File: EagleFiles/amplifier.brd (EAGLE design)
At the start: 100 x 80 mm, 52 parts, among them X1 736880-49

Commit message: Fix Feedback
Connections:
- removed net N$5: C2.-, R6.2, R7.1
- new net N$35: C2.+, EF86.3, R6.1
- new net N$36: EF86.8
- net N$3: now also C2.-, R6.2, R7.1; no longer C2.+, EF86.3, EF86.8, R6.1
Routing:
- net N$3: track 82.9 -> 32.7 mm
- net N$35: track 0.00 -> 49.0 mm, vias 0 -> 1
- net N$5: track 17.6 -> 0.00 mm
- net N$12: track 20.2 -> 26.5 mm
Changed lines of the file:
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@@
 <layer number="17" name="Pads" color="2" fill="1" visible="yes" active="yes"/>
 <layer number="18" name="Vias" color="2" fill="1" visible="yes" active="yes"/>
-<layer number="19" name="Unrouted" color="6" fill="1" visible="no" active="yes"/>
+<layer number="19" name="Unrouted" color="6" fill="1" visible="yes" active="yes"/>
 <layer number="20" name="Dimension" color="24" fill="1" visible="yes" active="yes"/>
 <layer number="21" name="tPlace" color="7" fill="1" visible="no" active="yes"/>
@@
 <wire x1="23.622" y1="25.146" x2="23.368" y2="24.826" width="1.016" layer="1"/>
 </signal>
-<signal name="N$3">
-<contactref element="EF86" pad="3"/>
-<contactref element="EF86" pad="8"/>
-<contactref element="R6" pad="1"/>
-<contactref element="R8" pad="1"/>
-<contactref element="C7" pad="1"/>
-<contactref element="C2" pad="+"/>
-<wire x1="15.24" y1="36.576" x2="15.24" y2="47.244" width="1.016" layer="1"/>
-<wire x1="19.812" y1="32.004" x2="15.24" y2="36.576" width="1.016" layer="1"/>
-<wire x1="15.24" y1="47.244" x2="14.633" y2="47.882" width="1.016" layer="1"/>
-<wire x1="19.812" y1="32.004" x2="20.137" y2="31.751" width="1.016" layer="1"/>
-<wire x1="36.576" y1="18.288" x2="32.766" y2="18.288" width="1.016" layer="1"/>
-<wire x1="32.766" y1="18.288" x2="32.512" y2="17.714" width="1.016" layer="1"/>
-<wire x1="36.576" y1="18.288" x2="37.084" y2="17.714" width="1.016" layer="1"/>
-<wire x1="44.196" y1="13.716" x2="47.752" y2="13.716" width="1.016" layer="1"/>
-<wire x1="40.386" y1="17.526" x2="44.196" y2="13.716" width="1.016" layer="1"/>
-<wire x1="37.338" y1="17.526" x2="40.386" y2="17.526" width="1.016" layer="1"/>
-<wire x1="37.338" y1="17.526" x2="37.084" y2="17.714" width="1.016" layer="1"/>
-<wire x1="41.402" y1="20.066" x2="47.752" y2="13.716" width="1.016" layer="16"/>
-<wire x1="41.402" y1="20.066" x2="31.242" y2="20.066" width="1.016" layer="16"/>
-<wire x1="20.574" y1="30.734" x2="20.574" y2="31.242" width="1.016" layer="16"/>
-<wire x1="28.702" y1="10.668" x2="28.702" y2="21.1836" width="1.016" layer="16"/>
-<wire x1="20.574" y1="31.242" x2="20.137" y2="31.751" width="1.016" layer="16"/>
-<wire x1="29.464" y1="21.844" x2="20.574" y2="30.734" width="1.016" layer="16"/>
-<wire x1="28.702" y1="21.1836" x2="29.3624" y2="21.844" width="1.016" layer="16"/>
-<wire x1="31.242" y1="20.066" x2="29.464" y2="21.844" width="1.016" layer="16"/>
-<wire x1="29.464" y1="21.844" x2="29.3624" y2="21.844" width="1.016" layer="16"/>
-</signal>
 <signal name="N$4">
 <contactref element="EF86" pad="1"/>
@@
 <wire x1="24.384" y1="44.958" x2="24.384" y2="45.085" width="1.016" layer="16"/>
 <wire x1="10.668" y1="35.052" x2="10.502" y2="34.874" width="1.016" layer="16"/>
-</signal>
-<signal name="N$5">
-<contactref element="R6" pad="2"/>
-<contactref element="R7" pad="1"/>
-<contactref element="C2" pad="-"/>
-<wire x1="34.29" y1="15.24" x2="32.766" y2="15.24" width="1.016" layer="1"/>
-<wire x1="38.862" y1="10.668" x2="34.29" y2="15.24" width="1.016" layer="1"/>
-<wire x1="32.766" y1="15.24" x2="32.512" y2="15.814" width="1.016" layer="1"/>
-<wire x1="28.194" y1="19.05" x2="25.334" y2="19.05" width="1.016" layer="1"/>
-<wire x1="32.004" y1="15.24" x2="28.194" y2="19.05" width="1.016" layer="1"/>
-<wire x1="32.004" y1="15.24" x2="32.512" y2="15.814" width="1.016" layer="1"/>
 </signal>
 <signal name="N$6">
@@
 </signal>
 <signal name="N$12">
-<contactref element="R8" pad="2"/>
-<contactref element="C7" pad="2"/>
 <contactref element="FEEDBACK" pad="1"/>
-<wire x1="40.386" y1="15.24" x2="37.338" y2="15.24" width="1.016" layer="1"/>
-<wire x1="47.244" y1="8.382" x2="40.386" y2="15.24" width="1.016" layer="1"/>
-<wire x1="37.338" y1="15.24" x2="37.084" y2="15.814" width="1.016" layer="1"/>
-<wire x1="47.244" y1="8.382" x2="47.752" y2="8.636" width="1.016" layer="1"/>
 <wire x1="48.006" y1="8.382" x2="48.006" y2="3.048" width="1.016" layer="1"/>
 <wire x1="48.006" y1="3.048" x2="48.26" y2="2.54" width="1.016" layer="1"/>
-<wire x1="48.006" y1="8.382" x2="47.752" y2="8.636" width="1.016" layer="1"/>
+<contactref element="C7" pad="2"/>
+<contactref element="R8" pad="2"/>
+<wire x1="47.752" y1="8.636" x2="50.038" y2="10.922" width="0.762" layer="1"/>
+<wire x1="50.038" y1="14.986" x2="49.53" y2="15.494" width="0.762" layer="1"/>
+<wire x1="37.404" y1="15.494" x2="37.084" y2="15.814" width="0.762" layer="1"/>
+<wire x1="50.038" y1="10.922" x2="50.038" y2="14.986" width="0.762" layer="1"/>
+<wire x1="49.53" y1="15.494" x2="37.404" y2="15.494" width="0.762" layer="1"/>
+<wire x1="48.006" y1="8.382" x2="47.752" y2="8.636" width="0" layer="19" extent="1-1"/>
 </signal>
 <signal name="N$13">
@@
 <via x="24.13" y="3.048" extent="1-16" drill="3" diameter="4.5"/>
 </signal>
+<signal name="N$35">
+<contactref element="EF86" pad="3"/>
+<contactref element="R6" pad="1"/>
+<contactref element="C2" pad="+"/>
+<wire x1="32.512" y1="17.714" x2="26.162" y2="24.064" width="0.762" layer="1"/>
+<wire x1="26.162" y1="24.064" x2="26.162" y2="39.878" width="0.762" layer="1"/>
+<wire x1="26.162" y1="39.878" x2="24.13" y2="41.91" width="0.762" layer="1"/>
+<wire x1="24.13" y1="41.91" x2="20.574" y2="41.91" width="0.762" layer="1"/>
+<wire x1="14.633" y1="47.851" x2="14.633" y2="47.882" width="0.762" layer="1"/>
+<wire x1="20.574" y1="41.91" x2="14.633" y2="47.851" width="0.762" layer="1"/>
+<wire x1="32.512" y1="17.714" x2="31.304784375" y2="17.714" width="0.762" layer="1"/>
+<wire x1="31.304784375" y1="17.714" x2="31.304784375" y2="13.270784375" width="0.762" layer="16"/>
+<wire x1="31.304784375" y1="13.270784375" x2="28.702" y2="10.668" width="0.762" layer="16"/>
+<via x="31.304784375" y="17.714" extent="1-16" drill="0.3048"/>
+</signal>
+<signal name="N$36">
+<contactref element="EF86" pad="8"/>
+</signal>
+<signal name="N$3">
+<contactref element="C7" pad="1"/>
+<contactref element="R8" pad="1"/>
+<contactref element="R6" pad="2"/>
+<contactref element="R7" pad="1"/>
+<contactref element="C2" pad="-"/>
+<wire x1="34.29" y1="15.24" x2="32.766" y2="15.24" width="1.016" layer="1"/>
+<wire x1="38.862" y1="10.668" x2="34.671" y2="14.859" width="1.016" layer="1"/>
+<wire x1="34.671" y1="14.859" x2="34.29" y2="15.24" width="1.016" layer="1"/>
+<wire x1="32.766" y1="15.24" x2="32.512" y2="15.814" width="1.016" layer="1"/>
+<wire x1="28.194" y1="19.05" x2="25.334" y2="19.05" width="1.016" layer="1"/>
+<wire x1="32.004" y1="15.24" x2="28.194" y2="19.05" width="1.016" layer="1"/>
+<wire x1="32.004" y1="15.24" x2="32.512" y2="15.814" width="1.016" layer="1"/>
+<wire x1="38.862" y1="10.668" x2="44.704" y2="10.668" width="0.762" layer="1"/>
+<wire x1="44.704" y1="10.668" x2="47.752" y2="13.716" width="0.762" layer="1"/>
+<wire x1="37.084" y1="17.714" x2="35.24" y2="17.714" width="0.762" layer="1"/>
+<wire x1="34.671" y1="17.145" x2="34.671" y2="14.859" width="0.762" layer="1"/>
+<wire x1="35.24" y1="17.714" x2="34.671" y2="17.145" width="0.762" layer="1"/>
+</signal>
 </signals>

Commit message: last not good design.
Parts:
- removed VSS: (no value), jumper:JP1
- removed X1: 736880-49, con-conrad:736880-49
- added GND_, INPUT: (no value), wirepad:2,54/1,0
- C1: device resistor:EB20D -> rcl:E5-13
- C12: value 100mF/100V -> 100u/100V; device rcl:E7,5-18 -> rcl:E5-10,5
- C2: value 10m/25V -> 10u/25V; device resistor:EB20D -> rcl:E5-8,5
- C3: value 10m -> 10u/450V; device resistor:EB20D -> rcl:E5-13
- C4: value 100uF/100V -> 100u/100V; device rcl:E7,5-18 -> rcl:E5-10,5
- C5: value 100nF -> 100n
- U$2, U$3: value KT88 -> KT88OKTAL1; device Tubes_all:OKTAL -> tubes_stockes:OKTAL1
- moved GND 101.6 mm to (97.4, 38.7)
- moved 12.6_EF86 88.3 mm to (86.5, 3.71), turned to 90 degrees
- moved U$2 81.6 mm to (17.5, 62.7), turned to 156 degrees
- moved 6.3_KT88 71.7 mm to (3.04, 49.3), turned to 0 degrees
- moved C3 68.9 mm to (7.70, 20.4), turned to 180 degrees
- moved KT88_TRAFO 67.4 mm to (43.2, 76.2), flipped to the bottom, turned to 90 degrees
- moved C11 64.9 mm to (8.12, 9.79), turned to 180 degrees
- moved 12.6V_ECC82 64.2 mm to (15.9, 3.26), turned to 90 degrees
- moved EF86 60.3 mm to (71.5, 13.0), turned to 180 degrees
- moved R15 57.3 mm to (33.8, 26.9), turned to 0 degrees
- moved C1 56.5 mm to (92.1, 12.2)
- moved ECC82 55.8 mm to (31.0, 13.0), turned to 180 degrees
- moved FEEDBACK 55.5 mm to (98.0, 27.3), turned to 90 degrees
- moved R8 55.5 mm to (91.3, 28.3)
- moved VDD 51.9 mm to (2.82, 40.4)
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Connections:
- removed net N$30: VSS.1, VSS.2
- removed net N$35: C2.+, EF86.3, R6.1
- net GND: now also GND_.1; no longer X1.1, X1.1@1, X1.1@2
- net N$1: now also INPUT.1; no longer X1.2
- net N$36: now also C2.+, EF86.3, R6.1
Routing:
- net N$36: track 0.00 -> 49.7 mm
- net N$35: track 49.0 -> 0.00 mm, vias 1 -> 0
- net N$7: track 77.6 -> 112.7 mm, vias 2 -> 0
- net N$15: track 27.2 -> 57.4 mm, vias 0 -> 1
- net N$34: track 70.6 -> 100.5 mm
- net KT88: track 17.7 -> 43.8 mm
- net N$17: track 40.6 -> 19.0 mm
- net N$33: track 89.4 -> 109.4 mm
- net N$14: track 47.5 -> 27.8 mm
- net N$18: track 67.2 -> 48.9 mm
- net KT88_2: track 60.7 -> 43.0 mm
- net N$10: track 48.5 -> 64.4 mm, vias 1 -> 0
- net N$23: track 19.2 -> 35.0 mm
- net N$3: track 32.7 -> 48.0 mm
- net N$6: track 56.7 -> 42.1 mm, vias 2 -> 0
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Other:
- board text added: "12.6V_ECC82"
- board text added: "INPUT"
- board text added: "Tosis V 1.1"
- board text removed: "12.6V ECC82"
- board text removed: "KT88"
- board text removed: "Tosis V 1.0"
- board text removed: "VSS"

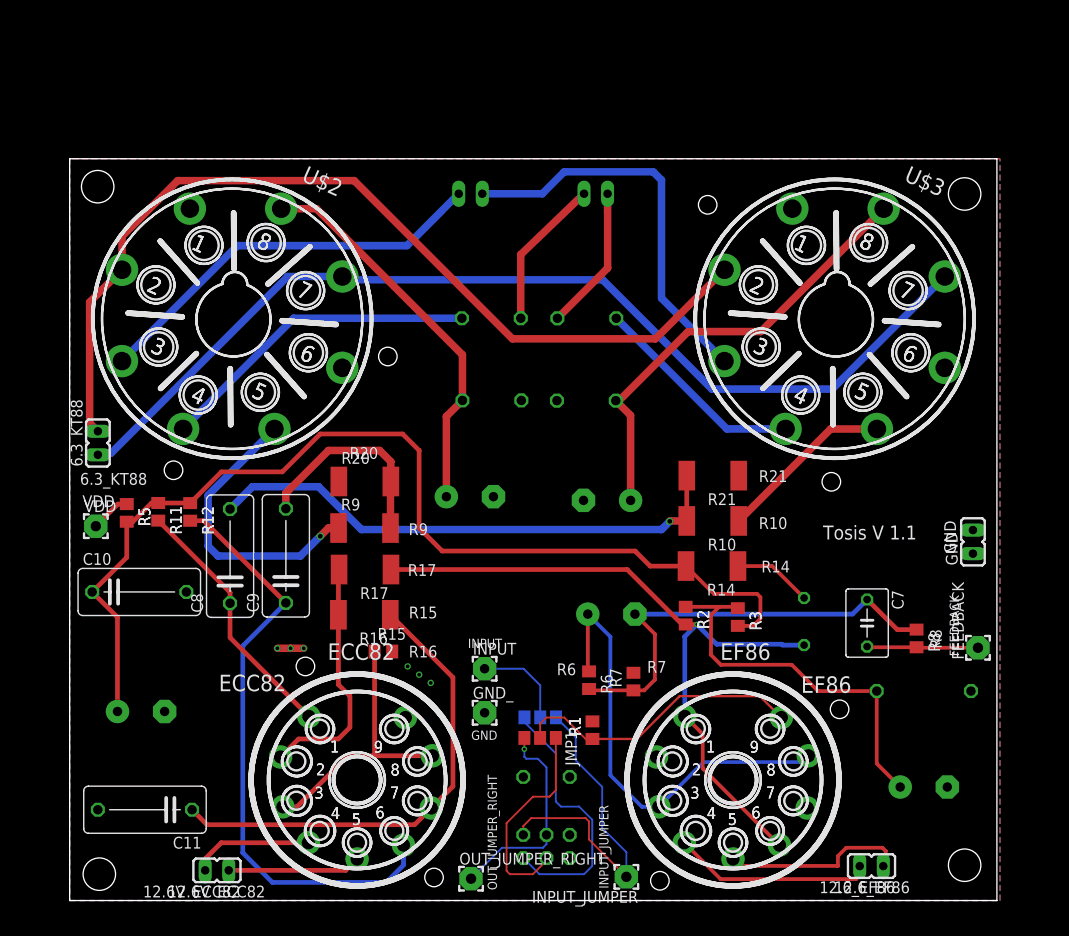
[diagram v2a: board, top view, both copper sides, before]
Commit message: back to old design, bigger dimensions and 2 feedbacks.
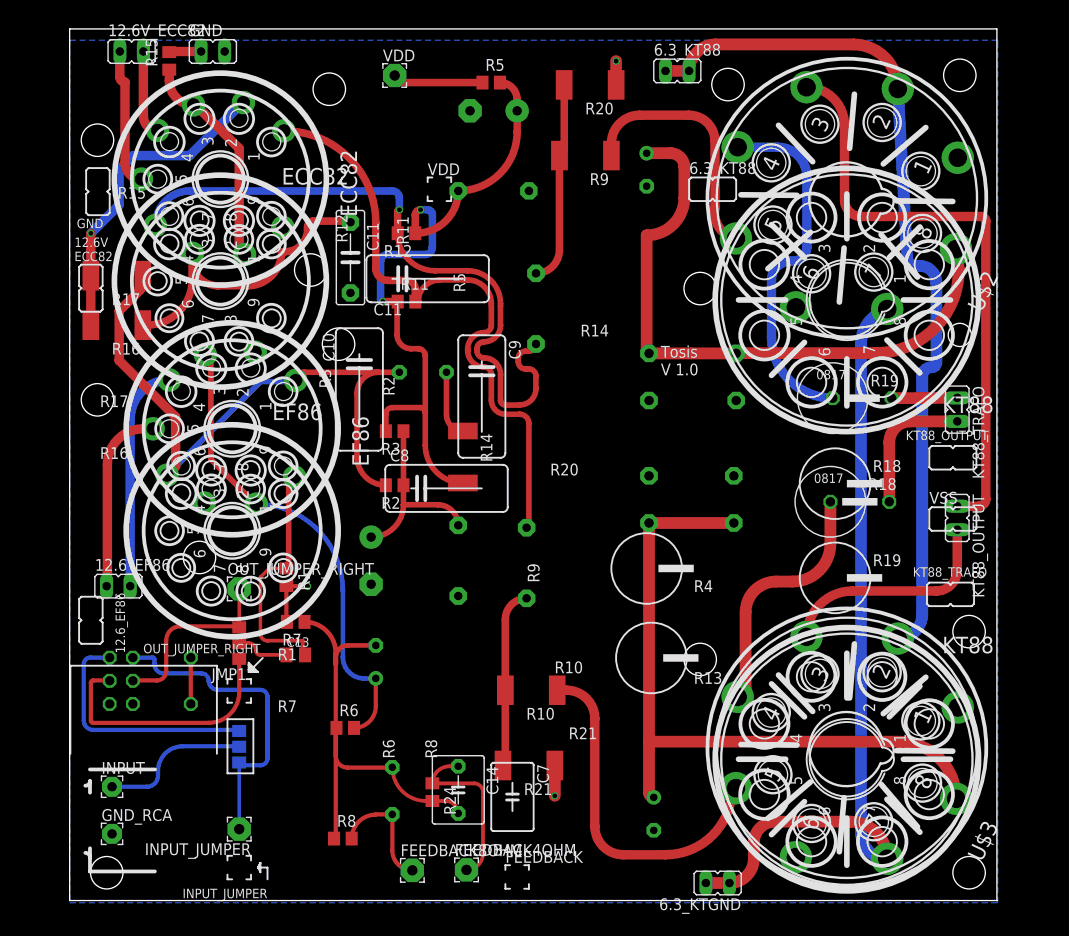
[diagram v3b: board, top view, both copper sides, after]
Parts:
- removed FEEDBACK: (no value), wirepad:2,54/1,1
- removed GND_: (no value), wirepad:2,54/1,0
- removed U$1: (no value), Bourns:PTR902-2015K-A104
- added 6.3_KTGND: 6.3 V, jumper:JP1
- added C13: 100nF, rcl:C0805K
- added C14: 680p, capacitor-wima:C5B5.5
- added FEEDBACK4OHM, FEEDBACK8OHM: (no value), wirepad:2,54/1,1
- added GND_RCA: WIREPAD2,15/1,0, wirepad:2,15/1,0
- added POT: 100K, Bourns:PTR902-2015K-A104
- added R22, R23: 470/5W, resistor_mod:0617V
- added R24: 5.6K, rcl:R0805
- C1, C3: device rcl:E5-13 -> rcl:E5-10,5
- C10, C11, C5: value 100n -> 100nF; device resistor:C102-054X133 -> capacitor-wima:C7.5B3
- C12, C4: value 100u/100V -> 100uF/100V; device rcl:E5-10,5 -> rcl:E3,5-10
- C2: device rcl:E5-8,5 -> rcl:E3,5-10
- C6, C7: device resistor:C050-045X075 -> capacitor-wima:C5B5.5
- C8, C9: value 220n -> 220nF; device resistor:C102-054X133 -> capacitor-wima:C7.5B3
- INPUT: value (none) -> WIREPAD2,15/1,0; device wirepad:2,54/1,0 -> wirepad:2,15/1,0
- R13, R4: value 220/5W -> 470/5W; device rcl:P0817V -> resistor_mod:0617V
- moved GND 97.5 mm to (15.4, 91.6), turned to 270 degrees
- moved 12.6V_ECC82 88.8 mm to (6.68, 91.6), turned to 270 degrees
- moved 12.6_EF86 86.7 mm to (5.26, 33.9), turned to 270 degrees
- moved C3 75.1 mm to (45.7, 85.2), turned to 0 degrees
- moved 6.3_KT88 74.3 mm to (65.5, 89.5), turned to 270 degrees
- moved R15 67.8 mm to (10.7, 90.6), turned to 90 degrees
- moved U$2 67.6 mm to (83.8, 75.8), turned to 65 degrees
- moved ECC82 66.5 mm to (16.3, 77.8), turned to 90 degrees
- moved EF86 66.0 mm to (17.5, 50.9), turned to 90 degrees
- moved R8 65.5 mm to (29.5, 6.68), turned to 0 degrees
- moved C1 64.4 mm to (32.5, 36.7), turned to 270 degrees
- moved C11 63.5 mm to (30.3, 69.3), turned to 270 degrees
- moved R5 60.8 mm to (45.5, 88.2), turned to 0 degrees
- moved VDD 58.3 mm to (35.1, 89.0)
- moved C10 57.7 mm to (45.7, 76.5), flipped to the bottom, turned to 180 degrees
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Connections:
- net N$10 renamed DIFFOUTPUT_P
- net N$14 renamed DIFFOUTPUT_N
- removed net N$36: C2.+, EF86.3, EF86.8, R6.1
- removed net N56: KT88_OUTPUT.2, R18.2
- new net N$10: C14.2, C2.-, C7.1, R24.2, R6.1, R7.1, R8.1
- new net N$14: C14.1, FEEDBACK4OHM.1, R24.1
- new net N$35: C13.1, JMP1.2
- new net N$56: KT88_TRAFO.2, R18.2
- net GND: now also GND_RCA.1, POT.R1_1, POT.R2_1, POT.SW1, POT.SW2, R22.2, R23.2; no longer GND_.1, U$1.R1_1, U$1.R2_1, U$1.SW1, U$1.SW2
- net KT88: now also KT88_OUTPUT.1; no longer KT88_TRAFO.1
- net KT88_2: now also KT88_OUTPUT.2; no longer KT88_TRAFO.2
- net N$12: now also FEEDBACK8OHM.1; no longer FEEDBACK.1
- net N$18: now also R23.1
- net N$19: now also R22.1
- net N$2: now also C13.2; no longer JMP1.2
- net N$21: now also POT.R1_2; no longer U$1.R1_2
- net N$22: now also POT.R1_3; no longer U$1.R1_3
- net N$26: now also POT.R2_2; no longer U$1.R2_2
- net N$27: now also KT88_TRAFO.1; no longer KT88_OUTPUT.1
- net N$28: now also POT.R2_3; no longer U$1.R2_3
- net N$3: now also C2.+, EF86.3, EF86.8; no longer C2.-, C7.1, R7.1, R8.1
- net N$33: now also 6.3_KTGND.1, 6.3_KTGND.2; no longer 6.3_KT88.1
- net N$34: now also 6.3_KT88.1
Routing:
- net N$36: track 49.7 -> 0.00 mm
- net N$10: track 0.00 -> 49.4 mm
- net N$7: track 112.7 -> 71.2 mm, vias 0 -> 2
- net N$15: track 57.4 -> 19.6 mm, vias 1 -> 0
- net DIFFOUTPUT_N: track 27.8 -> 64.7 mm
- net N$18: track 48.9 -> 74.6 mm
- net N$19: track 42.1 -> 65.9 mm
- net N$6: track 42.1 -> 19.7 mm
- net N$33: track 109.4 -> 87.9 mm
- net KT88: track 43.8 -> 63.4 mm
- net N$13: track 51.8 -> 32.3 mm
- net KT88_2: track 43.0 -> 23.6 mm
- net N$14: track 0.00 -> 18.5 mm
- net GND: track 2.84 -> 20.5 mm, vias 6 -> 3
- net N$17: track 19.0 -> 36.4 mm
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- removed copper zone on layer 1, net GND
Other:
- board size 100 x 80 mm -> 100 x 94 mm
- board text added: "12.6V ECC82"
- board text added: "KT88"
- board text added: "Tosis V 1.0"
- board text added: "VSS"
- board text removed: "12.6V_ECC82"
- board text removed: "INPUT"
- board text removed: "Tosis V 1.1"

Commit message: grid resistor closer to tube pins.
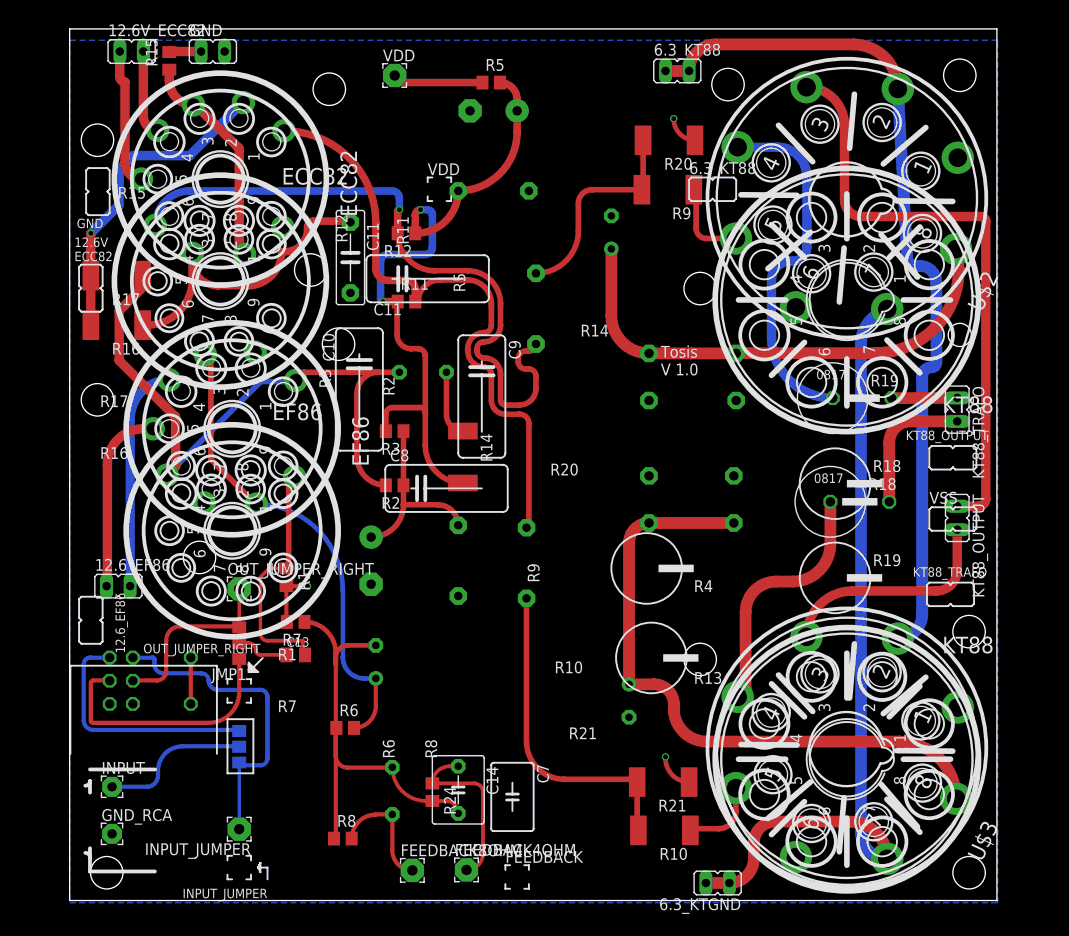
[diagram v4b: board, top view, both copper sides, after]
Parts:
- moved R10 20.8 mm to (64.1, 7.57)
- moved R21 14.6 mm to (64.0, 12.8)
- moved C4 12.5 mm to (60.3, 21.5)
- moved R20 10.4 mm to (64.6, 82.0)
- moved R9 9.62 mm to (64.5, 76.7)
- moved C12 7.76 mm to (58.4, 72.1), turned to 90 degrees
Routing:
- net N$17: track 36.4 -> 8.26 mm
- net N$16: track 26.1 -> 9.00 mm
- net N$15: track 19.6 -> 34.4 mm
- net N$19: track 65.9 -> 52.3 mm
- net N$18: track 74.6 -> 68.1 mm
- net GND: track 20.5 -> 21.7 mm
- net N$11: track 21.6 -> 22.3 mm
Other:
- board text removed: "C1"
- board text removed: "C12"
- board text removed: "C2"
- board text removed: "C3"
- board text removed: "C4"
- board text removed: "C5"
- board text removed: "C6"
